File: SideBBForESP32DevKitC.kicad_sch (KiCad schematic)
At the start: 4 parts, among them J1 Grove-I2C-connector, J2 mini-bread-board-1x17x2, J3 Grove-I2C-connector, U1 ESP32-DEVKITC-32D

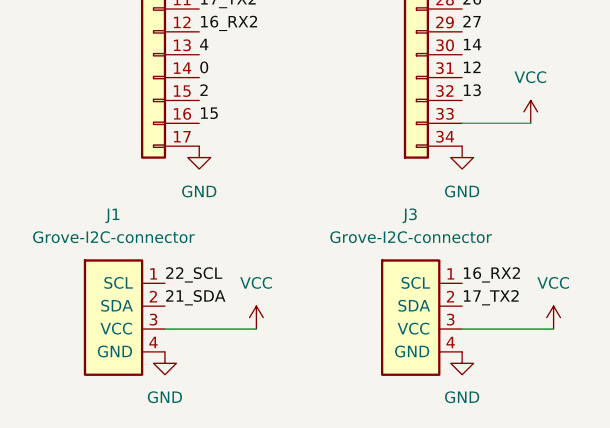
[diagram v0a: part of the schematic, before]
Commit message: Rename project name to SideBBForESP32DevKitC
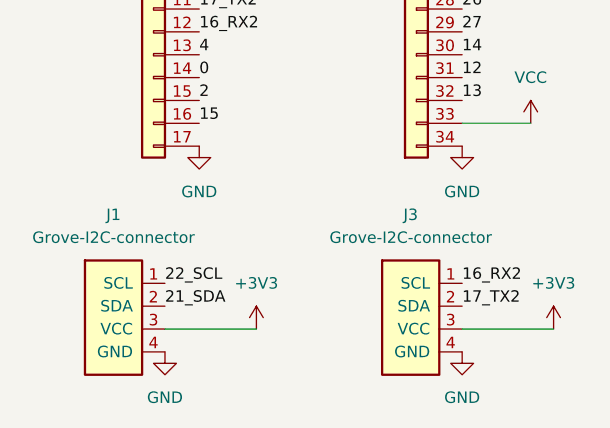
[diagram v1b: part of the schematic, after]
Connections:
- net +3V3: now also J1.3 (VCC), J3.3 (VCC)
- net VCC: no longer J1.3 (VCC), J3.3 (VCC)
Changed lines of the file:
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@@
     (effects (font (size 1.27 1.27)) (justify right bottom))
+  )
+  (symbol (lib_id "power:+3V3") (at 203.2 132.08 0) (unit 1)
+    (in_bom yes) (on_board yes)
+    (property "Reference" "#PWR?" (id 0) (at 203.2 135.89 0)
+      (effects (font (size 1.27 1.27)) hide)
+    )
+    (property "Value" "+3V3" (id 1) (at 203.2 127 0))
+    (property "Footprint" "" (id 2) (at 203.2 132.08 0)
+      (effects (font (size 1.27 1.27)) hide)
+    )
+    (property "Datasheet" "" (id 3) (at 203.2 132.08 0)
+      (effects (font (size 1.27 1.27)) hide)
+    )
+    (pin "1")
   )
   (symbol (lib_id "power:GND") (at 226.06 134.62 0) (unit 1)
@@
     )
     (property "Datasheet" "" (id 3) (at 237.49 71.12 0)
-      (effects (font (size 1.27 1.27)) hide)
-    )
-    (pin "1")
-  )
-  (symbol (lib_id "power:VCC") (at 203.2 132.08 0) (unit 1)
-    (in_bom yes) (on_board yes) (fields_autoplaced)
-    (property "Reference" "#PWR0109" (id 0) (at 203.2 135.89 0)
-      (effects (font (size 1.27 1.27)) hide)
-    )
-    (property "Value" "VCC" (id 1) (at 203.2 127 0))
-    (property "Footprint" "" (id 2) (at 203.2 132.08 0)
-      (effects (font (size 1.27 1.27)) hide)
-    )
-    (property "Datasheet" "" (id 3) (at 203.2 132.08 0)
       (effects (font (size 1.27 1.27)) hide)
     )
@@
     (pin "3")
     (pin "4")
-  )
-  (symbol (lib_id "power:VCC") (at 236.22 132.08 0) (unit 1)
-    (in_bom yes) (on_board yes) (fields_autoplaced)
-    (property "Reference" "#PWR0113" (id 0) (at 236.22 135.89 0)
-      (effects (font (size 1.27 1.27)) hide)
-    )
-    (property "Value" "VCC" (id 1) (at 236.22 127 0))
-    (property "Footprint" "" (id 2) (at 236.22 132.08 0)
-      (effects (font (size 1.27 1.27)) hide)
-    )
-    (property "Datasheet" "" (id 3) (at 236.22 132.08 0)
-      (effects (font (size 1.27 1.27)) hide)
-    )
-    (pin "1")
   )
   (symbol (lib_id "asukiaaa-kicad-symbols:Grove-I2C-connector") (at 186.69 130.81 0) (unit 1)
@@
     (pin "34")
   )
+  (symbol (lib_id "power:+3V3") (at 236.22 132.08 0) (unit 1)
+    (in_bom yes) (on_board yes)
+    (property "Reference" "#PWR?" (id 0) (at 236.22 135.89 0)
+      (effects (font (size 1.27 1.27)) hide)
+    )
+    (property "Value" "+3V3" (id 1) (at 236.22 127 0))
+    (property "Footprint" "" (id 2) (at 236.22 132.08 0)
+      (effects (font (size 1.27 1.27)) hide)
+    )
+    (property "Datasheet" "" (id 3) (at 236.22 132.08 0)
+      (effects (font (size 1.27 1.27)) hide)
+    )
+    (pin "1")
+  )
   (symbol (lib_id "power:+3V3") (at 237.49 86.36 0) (unit 1)
     (in_bom yes) (on_board yes)
@@
       (reference "#PWR0108") (unit 1) (value "GND") (footprint "")
     )
-    (path "/6906f1a8-5cdf-498a-bfa6-4275c1d4e03b"
-      (reference "#PWR0109") (unit 1) (value "VCC") (footprint "")
-    )
     (path "/d08d4d49-b388-4892-8323-51109b3e6892"
       (reference "#PWR0110") (unit 1) (value "GND") (footprint "")
@@
       (reference "#PWR0112") (unit 1) (value "+3V3") (footprint "")
     )
-    (path "/90871ced-792e-45f5-b74e-584f9a150cb4"
-      (reference "#PWR0113") (unit 1) (value "VCC") (footprint "")
-    )
     (path "/16010e58-8aee-45c1-99df-d1cc2bd80779"
       (reference "#PWR0114") (unit 1) (value "GND") (footprint "")
     )
+    (path "/125b7ac6-58f8-4648-989a-7cb26078849e"
+      (reference "#PWR?") (unit 1) (value "+3V3") (footprint "")
+    )
+    (path "/c40d36bb-2efa-4bc3-859b-223faaa66f3e"
+      (reference "#PWR?") (unit 1) (value "+3V3") (footprint "")
+    )
     (path "/9a8b7046-99b9-43b5-9740-2bf42c50fd1e"
